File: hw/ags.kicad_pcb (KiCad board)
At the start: 4 copper layers, 0 parts

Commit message: Footprints created, starting layout
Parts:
- added C1: 22u, Capacitor_SMD:C_0603_1608Metric, F.Cu at (201.8, 34.2)
- added C10: 1u, Capacitor_SMD:C_0603_1608Metric, F.Cu at (232.0, 80.6)
- added C11: 2.7n, Capacitor_SMD:C_0603_1608Metric, F.Cu at (232.0, 83.1)
- added C12: 1u, Capacitor_SMD:C_0603_1608Metric, F.Cu at (211.8, 100.0)
- added C13: 1u, Capacitor_SMD:C_0603_1608Metric, F.Cu at (232.0, 61.1)
- added C14: 2.7n, Capacitor_SMD:C_0603_1608Metric, F.Cu at (232.0, 63.7)
- added C15: 2.7n, Capacitor_SMD:C_0603_1608Metric, F.Cu at (211.8, 102.5)
- added C16: 1u, Capacitor_SMD:C_0603_1608Metric, F.Cu at (211.8, 80.6)
- added C17: 2.7n, Capacitor_SMD:C_0603_1608Metric, F.Cu at (211.8, 83.1)
- added C18: 1u, Capacitor_SMD:C_0603_1608Metric, F.Cu at (211.8, 61.1)
- added C19: 2.7n, Capacitor_SMD:C_0603_1608Metric, F.Cu at (211.8, 63.7)
- added C2: 100n, Capacitor_SMD:C_0603_1608Metric, F.Cu at (201.8, 36.7)
- added C20: 1u, Capacitor_SMD:C_0603_1608Metric, F.Cu at (175.6, 92.9)
- added C21: 2.7n, Capacitor_SMD:C_0603_1608Metric, F.Cu at (175.6, 95.4)
- added C22: 1u, Capacitor_SMD:C_0603_1608Metric, F.Cu at (232.0, 100.0)
- added C23: 2.7n, Capacitor_SMD:C_0603_1608Metric, F.Cu at (232.0, 102.5)
- added C24: 100n, Capacitor_SMD:C_0603_1608Metric, F.Cu at (224.9, 39.2)
- added C3: 1u, Capacitor_SMD:C_0603_1608Metric, F.Cu at (201.8, 39.2)
- added C4: 1u, Capacitor_SMD:C_0603_1608Metric, F.Cu at (201.8, 41.7)
- added C5: 1u, Capacitor_SMD:C_0603_1608Metric, F.Cu at (155.3, 92.9)
- added C6: 4.7u, Capacitor_SMD:C_1210_3225Metric, F.Cu at (230.9, 54.6)
- added C7: 100n, Capacitor_SMD:C_0603_1608Metric, F.Cu at (224.9, 34.2)
- added C8: 22u, Capacitor_SMD:C_0603_1608Metric, F.Cu at (224.9, 36.7)
- added C9: 2.7n, Capacitor_SMD:C_0603_1608Metric, F.Cu at (155.3, 95.4)
- added D1: B38G3RGB-10D0003H2U1930, qmi_footprints:B38G3RGB-10D0003H2U1930, F.Cu at (201.1, 50.2)
- added D10: SMAJ60CA, Diode_SMD:D_SMA, F.Cu at (217.9, 113.8)
- added D11: SM4007PL, Diode_SMD:D_SOD-123F, F.Cu at (225.3, 88.0)
- added D12: SMAJ60CA, Diode_SMD:D_SMA, F.Cu at (217.9, 94.4)
- added D13: SM4007PL, Diode_SMD:D_SOD-123F, F.Cu at (225.3, 68.6)
- added D14: SMAJ60CA, Diode_SMD:D_SMA, F.Cu at (217.9, 75.0)
- added D15: SM4007PL, Diode_SMD:D_SOD-123F, F.Cu at (189.1, 100.3)
- added D16: SMAJ60CA, Diode_SMD:D_SMA, F.Cu at (181.6, 106.8)
- added D17: SM4007PL, Diode_SMD:D_SOD-123F, F.Cu at (245.6, 107.4)
- added D18: SMAJ60CA, Diode_SMD:D_SMA, F.Cu at (238.1, 113.8)
- added D19: SM4007PL, Diode_SMD:D_SOD-123F, F.Cu at (245.6, 71.9)
- added D2: SMAJ60CA, Diode_SMD:D_SMA, F.Cu at (238.1, 75.0)
- added D20: SM4007PL, Diode_SMD:D_SOD-123F, F.Cu at (168.8, 103.7)
- added D21: SM4007PL, Diode_SMD:D_SOD-123F, F.Cu at (245.6, 91.3)
- added D22: SM4007PL, Diode_SMD:D_SOD-123F, F.Cu at (225.3, 110.8)
- added D23: SM4007PL, Diode_SMD:D_SOD-123F, F.Cu at (225.3, 91.3)
- added D24: SM4007PL, Diode_SMD:D_SOD-123F, F.Cu at (225.3, 71.9)
- added D25: SM4007PL, Diode_SMD:D_SOD-123F, F.Cu at (189.1, 103.7)
- added D26: SM4007PL, Diode_SMD:D_SOD-123F, F.Cu at (245.6, 110.8)
- added D27: SM4007PL, Diode_SMD:D_SOD-123F, F.Cu at (229.7, 42.7)
- added D3: SM4007PL, Diode_SMD:D_SOD-123F, F.Cu at (245.6, 68.6)
- added D4: SMAJ60CA, Diode_SMD:D_SMA, F.Cu at (213.8, 55.6)
- added D5: SM4007PL, Diode_SMD:D_SOD-123F, F.Cu at (168.8, 100.3)
- added D6: SMAJ60CA, Diode_SMD:D_SMA, F.Cu at (161.4, 106.8)
- added D7: SM4007PL, Diode_SMD:D_SOD-123F, F.Cu at (245.6, 88.0)
- added D8: SM4007PL, Diode_SMD:D_SOD-123F, F.Cu at (225.3, 107.4)
- added D9: SMAJ60CA, Diode_SMD:D_SMA, F.Cu at (238.1, 94.4)
- added F1: 0ZCF0075AF2C, Fuse:Fuse_2920_7451Metric, F.Cu at (228.0, 49.0)
- added F2: 0ZCF0075AF2C, Fuse:Fuse_2920_7451Metric, F.Cu at (239.2, 63.4)
- added F3: 0ZCF0075AF2C, Fuse:Fuse_2920_7451Metric, F.Cu at (162.4, 95.2)
- added F4: 0ZCF0075AF2C, Fuse:Fuse_2920_7451Metric, F.Cu at (239.2, 82.8)
- added F5: 0ZCF0075AF2C, Fuse:Fuse_2920_7451Metric, F.Cu at (218.9, 102.2)
- added F6: 0ZCF0075AF2C, Fuse:Fuse_2920_7451Metric, F.Cu at (218.9, 82.8)
- added F7: 0ZCF0075AF2C, Fuse:Fuse_2920_7451Metric, F.Cu at (218.9, 63.4)
- added F8: 0ZCF0075AF2C, Fuse:Fuse_2920_7451Metric, F.Cu at (182.7, 95.2)
- added F9: 0ZCF0075AF2C, Fuse:Fuse_2920_7451Metric, F.Cu at (239.2, 102.2)
- added J1: Screw_Terminal_01x08, qmi_footprints:QT08ASF83H0000G, F.Cu at (166.9, 132.4)
- added J9: Screw_Terminal_01x02, qmi_footprints:QT02ASF83H0000G, F.Cu at (121.9, 128.9)
- added L1: 22u HPC 6045NV-220M, qmi_footprints:HPC 6045NV-220M, F.Cu at (231.0, 37.0)
- added R1: 1k, Resistor_SMD:R_0603_1608Metric, F.Cu at (201.8, 44.2)
- added R10: 270, Resistor_SMD:R_0603_1608Metric, F.Cu at (211.8, 105.0)
- added R11: 270, Resistor_SMD:R_0603_1608Metric, F.Cu at (232.0, 66.2)
- added R12: 113k 1%, Resistor_SMD:R_0603_1608Metric, F.Cu at (211.8, 107.5)
- added R13: 113k 1%, Resistor_SMD:R_0603_1608Metric, F.Cu at (232.0, 68.7)
- added R14: 32k 1%, Resistor_SMD:R_0603_1608Metric, F.Cu at (224.9, 41.7)
- added R15: 5.90k 1%, Resistor_SMD:R_0603_1608Metric, F.Cu at (201.8, 46.7)
- added R16: 5.90k 1%, Resistor_SMD:R_0603_1608Metric, F.Cu at (211.8, 110.0)
- added R17: 100 ERJ-P06F1000V, Resistor_SMD:R_0805_2012Metric, F.Cu at (224.7, 113.9)
- added R18: 5.90k 1%, Resistor_SMD:R_0603_1608Metric, F.Cu at (232.0, 71.2)
- added R19: 5.90k 1%, Resistor_SMD:R_0603_1608Metric, F.Cu at (205.8, 34.2)
- added R2: 270, Resistor_SMD:R_0603_1608Metric, F.Cu at (155.3, 97.9)
- added R20: 100 ERJ-P06F1000V, Resistor_SMD:R_0805_2012Metric, F.Cu at (245.0, 75.1)
- added R21: 270, Resistor_SMD:R_0603_1608Metric, F.Cu at (211.8, 85.6)
- added R22: 113k 1%, Resistor_SMD:R_0603_1608Metric, F.Cu at (211.8, 88.1)
- added R23: 5.90k 1%, Resistor_SMD:R_0603_1608Metric, F.Cu at (211.8, 90.6)
- added R24: 100 ERJ-P06F1000V, Resistor_SMD:R_0805_2012Metric, F.Cu at (224.7, 94.5)
- added R25: 270, Resistor_SMD:R_0603_1608Metric, F.Cu at (211.8, 66.2)
- added R26: 113k 1%, Resistor_SMD:R_0603_1608Metric, F.Cu at (211.8, 68.7)
- added R27: 5.90k 1%, Resistor_SMD:R_0603_1608Metric, F.Cu at (211.8, 71.2)
- added R28: 100 ERJ-P06F1000V, Resistor_SMD:R_0805_2012Metric, F.Cu at (224.7, 75.1)
- added R29: 270, Resistor_SMD:R_0603_1608Metric, F.Cu at (175.6, 97.9)
- added R3: 113k 1%, Resistor_SMD:R_0603_1608Metric, F.Cu at (155.3, 100.4)
- added R30: 113k 1%, Resistor_SMD:R_0603_1608Metric, F.Cu at (175.6, 100.4)
- added R31: 5.90k 1%, Resistor_SMD:R_0603_1608Metric, F.Cu at (175.6, 102.9)
- added R32: 100 ERJ-P06F1000V, Resistor_SMD:R_0805_2012Metric, F.Cu at (188.5, 106.8)
- added R33: 270, Resistor_SMD:R_0603_1608Metric, F.Cu at (232.0, 105.0)
- added R34: 113k 1%, Resistor_SMD:R_0603_1608Metric, F.Cu at (232.0, 107.5)
- added R35: 5.90k 1%, Resistor_SMD:R_0603_1608Metric, F.Cu at (232.0, 110.0)
- added R36: 100 ERJ-P06F1000V, Resistor_SMD:R_0805_2012Metric, F.Cu at (245.0, 113.9)
- added R37: 1k, Resistor_SMD:R_0603_1608Metric, F.Cu at (205.8, 36.7)
- added R38: 1k, Resistor_SMD:R_0603_1608Metric, F.Cu at (205.8, 39.2)
- added R39: 1k, Resistor_SMD:R_0603_1608Metric, F.Cu at (205.8, 41.7)
- added R4: 5.90k 1%, Resistor_SMD:R_0603_1608Metric, F.Cu at (155.3, 102.9)
- added R40: 270, Resistor_SMD:R_0603_1608Metric, F.Cu at (205.8, 44.2)
- added R41: 100k 1%, Resistor_SMD:R_0603_1608Metric, F.Cu at (224.9, 44.2)
- added R5: 100 ERJ-P06F1000V, Resistor_SMD:R_0805_2012Metric, F.Cu at (168.3, 106.8)
- added R6: 270, Resistor_SMD:R_0603_1608Metric, F.Cu at (232.0, 85.6)
- added R7: 113k 1%, Resistor_SMD:R_0603_1608Metric, F.Cu at (232.0, 88.1)
- added R8: 5.90k 1%, Resistor_SMD:R_0603_1608Metric, F.Cu at (232.0, 90.6)
- added R9: 100 ERJ-P06F1000V, Resistor_SMD:R_0805_2012Metric, F.Cu at (245.0, 94.5)
- added SW1: PTS526SM15SMTR2 LFS, qmi_footprints:SON4_PTS526 SM15 SMTR2 LFS_CNK, F.Cu at (200.9, 72.8)
- added U1: GAQY212GSX, Package_SO:SO-4_4.4x4.3mm_P2.54mm, F.Cu at (161.7, 101.6)
- added U10: GAQY212GSX, Package_SO:SO-4_4.4x4.3mm_P2.54mm, F.Cu at (181.9, 101.6)
- added U11: GAQY212GSX, Package_SO:SO-4_4.4x4.3mm_P2.54mm, F.Cu at (238.4, 108.7)
- added U12: NV24C08DWVLT3G, Package_SO:SOIC-8_3.9x4.9mm_P1.27mm, F.Cu at (200.6, 79.7)
- added U2: GAQY212GSX, Package_SO:SO-4_4.4x4.3mm_P2.54mm, F.Cu at (238.4, 89.2)
- added U3: GAQY212GSX, Package_SO:SO-4_4.4x4.3mm_P2.54mm, F.Cu at (218.2, 108.7)
- added U4: LMR51610XDBVR, Package_TO_SOT_SMD:SOT-23-6, F.Cu at (225.5, 54.9)
- added U5: ESP32-S3-MINI-1, RF_Module:ESP32-S2-MINI-1, F.Cu at (150.2, 66.2)
- added U6: GAQY212GSX, Package_SO:SO-4_4.4x4.3mm_P2.54mm, F.Cu at (238.4, 69.8)
- added U7: GAQY212GSX, Package_SO:SO-4_4.4x4.3mm_P2.54mm, F.Cu at (218.2, 89.2)
- added U9: GAQY212GSX, Package_SO:SO-4_4.4x4.3mm_P2.54mm, F.Cu at (218.2, 69.8)

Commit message: Initial start to PCB
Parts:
- moved D6 92.3 mm to (238.6, 157.3)
- moved D5 92.3 mm to (246.1, 150.8)
- moved R2 92.3 mm to (232.6, 148.4)
- moved R29 92.3 mm to (252.8, 148.4)
- moved R5 92.3 mm to (245.5, 157.3)
- moved U1 92.3 mm to (238.9, 152.1)
- moved U10 92.3 mm to (259.2, 152.1)
- moved C20 92.3 mm to (252.8, 143.4)
- moved C21 92.3 mm to (252.8, 145.9)
- moved C5 92.3 mm to (232.6, 143.4)
- moved C9 92.3 mm to (232.6, 145.9)
- moved D16 92.3 mm to (258.9, 157.3)
- moved D20 92.3 mm to (246.1, 154.2)
- moved F3 92.3 mm to (239.7, 145.6)
- moved F8 92.3 mm to (259.9, 145.6)
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
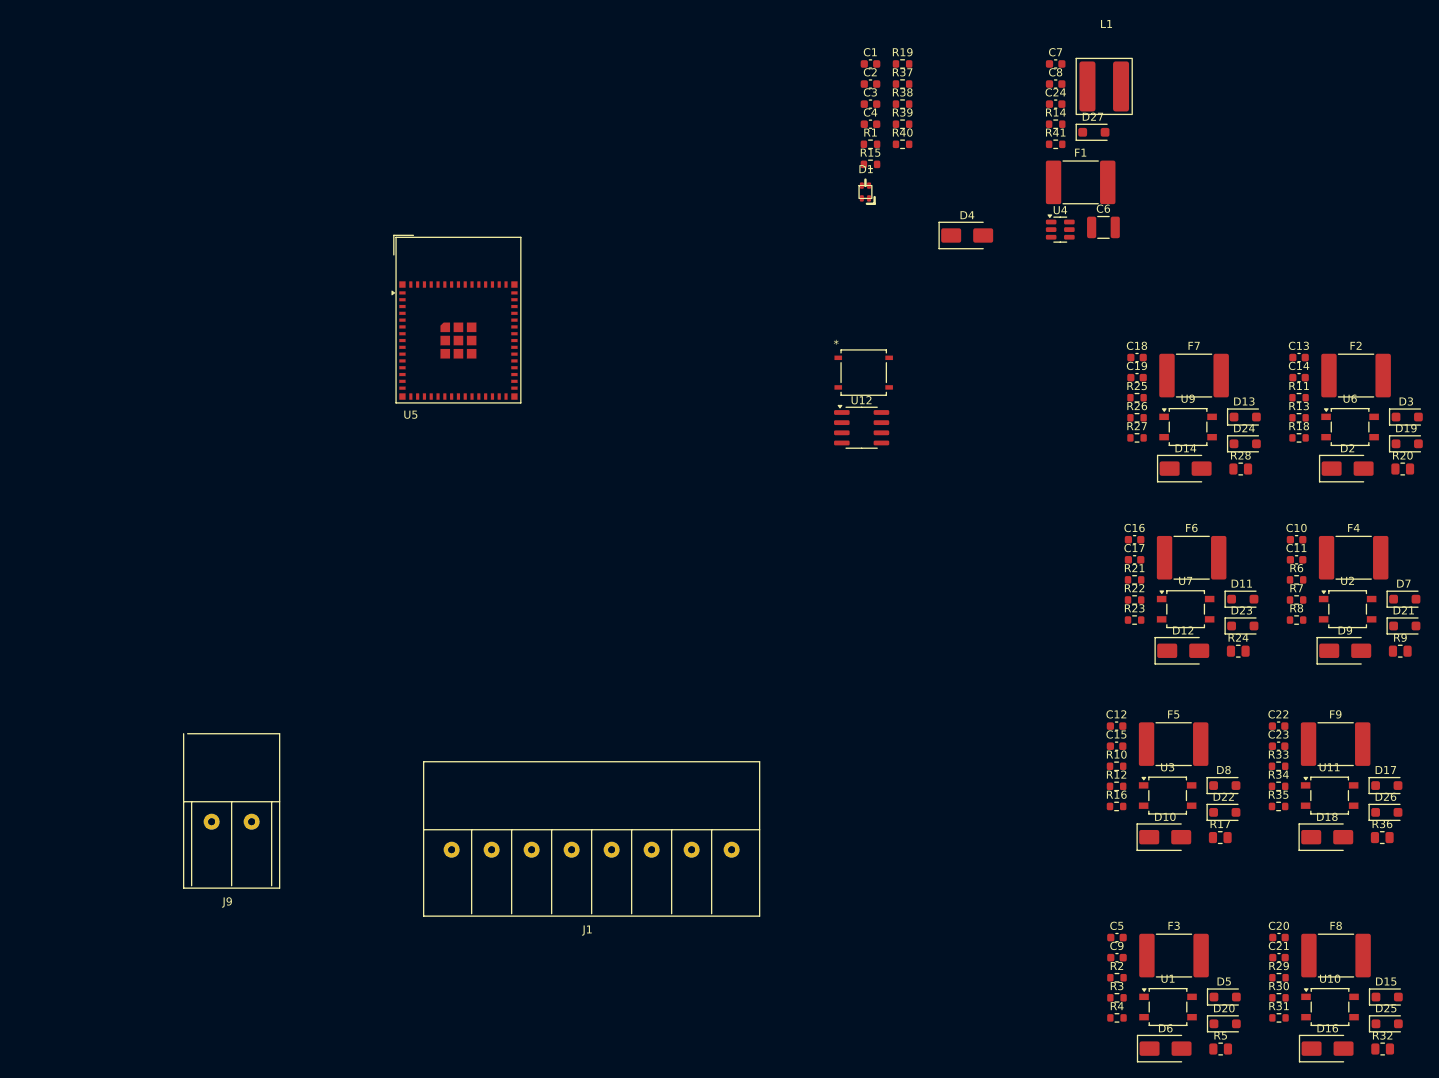
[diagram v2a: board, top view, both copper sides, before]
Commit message: All parts placed and routed
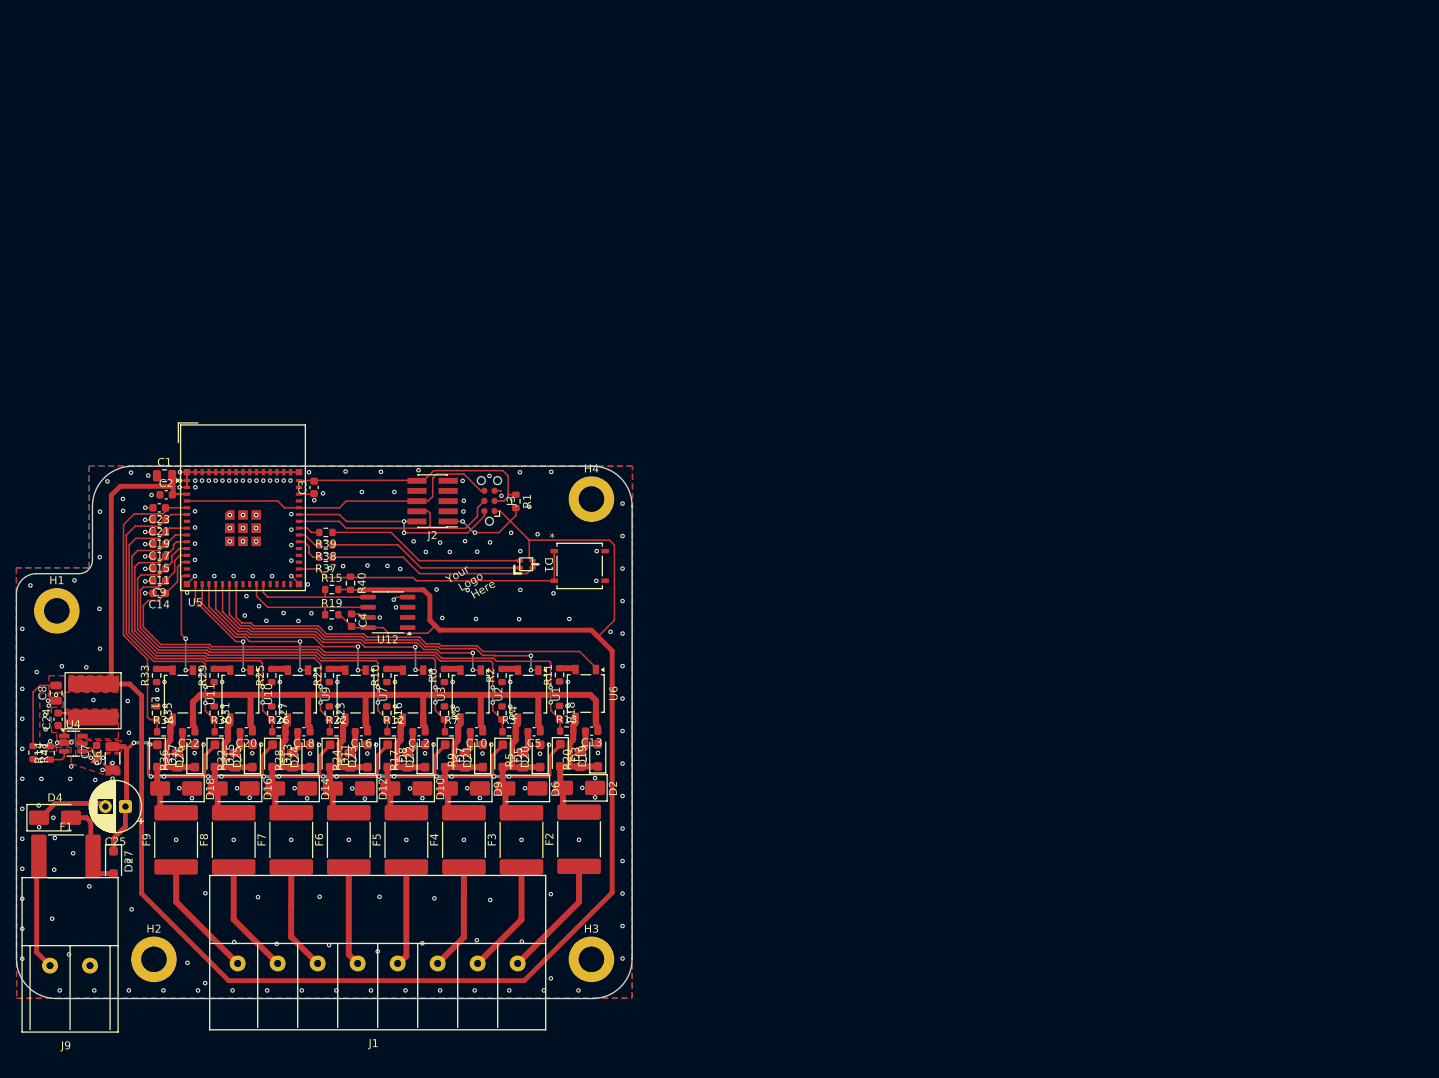
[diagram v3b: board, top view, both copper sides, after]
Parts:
- added C25: 22u, Capacitor_THT:CP_Radial_D6.3mm_P2.50mm, F.Cu at (108.6, 127.0)
- added H1: MountingHole_Pad, MountingHole:MountingHole_3.2mm_M3_ISO7380_Pad, F.Cu at (100.1, 102.5)
- added H2: MountingHole_Pad, MountingHole:MountingHole_3.2mm_M3_ISO7380_Pad, F.Cu at (112.2, 146.1)
- added H3: MountingHole_Pad, MountingHole:MountingHole_3.2mm_M3_ISO7380_Pad, F.Cu at (166.9, 146.1)
- added H4: MountingHole_Pad, MountingHole:MountingHole_3.2mm_M3_ISO7380_Pad, F.Cu at (166.9, 88.6)
- added J2: SWD/ARM10, Connector_PinHeader_1.27mm:PinHeader_2x05_P1.27mm_Vertical_SMD, F.Cu at (147.0, 88.8)
- added J3: Conn_02x03_Odd_Even, Connector:Tag-Connect_TC2030-IDC-NL_2x03_P1.27mm_Vertical, F.Cu at (154.1, 88.8)
- C1, C8: footprint Capacitor_SMD:C_0603_1608Metric -> Capacitor_SMD:C_0805_2012Metric
- C6: footprint Capacitor_SMD:C_1210_3225Metric -> Capacitor_SMD:C_1206_3216Metric
- R1: value 1k -> 5.90k 1%
- moved D17 153.7 mm to (112.6, 120.7), turned to -90 degrees
- moved D27 152.8 mm to (107.1, 134.0), turned to -90 degrees
- moved F1 152.3 mm to (101.2, 133.2)
- moved R36 150.9 mm to (115.1, 121.2), turned to 90 degrees
- moved C21 150.3 mm to (112.9, 91.2), turned to 180 degrees
- moved D15 149.6 mm to (119.8, 120.7), turned to -90 degrees
- moved D26 149.2 mm to (117.3, 120.7), turned to 90 degrees
- moved R41 148.7 mm to (97.1, 120.3), turned to -90 degrees
- moved R14 148.2 mm to (99.2, 120.3), turned to 90 degrees
- moved R32 147.9 mm to (122.3, 121.2), turned to 90 degrees
- moved L1 147.9 mm to (104.6, 113.8), turned to -90 degrees
- moved C7 147.5 mm to (105.0, 120.1), turned to 90 degrees
- moved C24 146.5 mm to (100.2, 116.1), turned to 90 degrees
- moved C8 146.3 mm to (100.0, 112.8), turned to 90 degrees
- moved D25 145.7 mm to (124.5, 120.7), turned to 90 degrees
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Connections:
- net Net-(U5-EN) renamed /ESP_EN
- R40 pad 1: Net-(U5-IO48) -> Net-(U5-IO36)
- SW1 pad 1: Net-(U5-IO48) -> Net-(U5-IO36)
- SW1 pad 2: Net-(U5-IO48) -> Net-(U5-IO36)
- U5 pad 10: /SENSE_5 -> /SENSE_4
- U5 pad 11: /SENSE_6 -> /SENSE_3
- U5 pad 12: /SENSE_7 -> /SENSE_2
- U5 pad 13: /SENSE_8 -> /SENSE_1
- U5 pad 15: /EN_1 -> /EN_8
- U5 pad 16: /EN_2 -> /EN_7
- U5 pad 17: /EN_3 -> /EN_6
- U5 pad 18: /EN_4 -> /EN_5
- U5 pad 19: /EN_5 -> /EN_4
- U5 pad 20: /EN_6 -> /EN_3
- U5 pad 21: /EN_7 -> /EN_2
- U5 pad 22: /EN_8 -> /EN_1
- U5 pad 30: Net-(U5-IO48) -> unconnected-(U5-IO48-Pad30)
- U5 pad 32: unconnected-(U5-IO36-Pad32) -> Net-(U5-IO36)
- U5 pad 39: unconnected-(U5-TXD0-Pad39) -> /TX
- U5 pad 4: unconnected-(U5-IO0-Pad4) -> /IO0
- U5 pad 40: unconnected-(U5-RXD0-Pad40) -> /RX
- U5 pad 41: unconnected-(U5-IO45-Pad41) -> /IO0
- U5 pad 5: /SENSE_1 -> /SENSE_8
- U5 pad 6: /SENSE_2 -> /SENSE_7
- U5 pad 8: /SENSE_3 -> /SENSE_6
- U5 pad 9: /SENSE_4 -> /SENSE_5
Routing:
- net +3.3V: track 0.00 -> 275.6 mm, vias 0 -> 2
- net +V: track 0.00 -> 108.4 mm, vias 0 -> 16
- net /COMM_V: track 0.00 -> 86.7 mm
- net /SENSE_1: track 0.00 -> 73.3 mm, vias 0 -> 2
- net /SENSE_2: track 0.00 -> 68.1 mm, vias 0 -> 2
- net GND: track 0.00 -> 63.2 mm, vias 0 -> 270
- net /SENSE_3: track 0.00 -> 62.4 mm, vias 0 -> 2
- net /SENSE_4: track 0.00 -> 56.9 mm, vias 0 -> 2
- net /EN_1: track 0.00 -> 51.9 mm
- net /SENSE_5: track 0.00 -> 51.4 mm, vias 0 -> 2
- net /EN_2: track 0.00 -> 46.4 mm, vias 0 -> 2
- net /SENSE_6: track 0.00 -> 46.1 mm, vias 0 -> 2
- net /IO0: track 0.00 -> 41.5 mm
- net /SENSE_7: track 0.00 -> 41.4 mm, vias 0 -> 2
- net /EN_3: track 0.00 -> 40.0 mm, vias 0 -> 2
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- added copper zone on F.Cu, net +3.3V
- added copper zone on F.Cu, net +V
- added copper zone on B.Cu, net GND
- added copper zone on F.Cu, net GND
- added copper zone on F.Cu, net Net-(U4-SW)
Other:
- board outline added: 77 x 66.5 mm
- copper layers 4 -> 2
- board text added: "Your Logo Here"
